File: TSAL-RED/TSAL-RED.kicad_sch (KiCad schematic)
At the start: 41 parts, among them J1 Conn_01x02, J2 Conn_01x02, J5 Conn_02x01, J6 Conn_02x03_Counter_Clockwise, K1 G5V-2, Q1 2N7002, Q2 AO3401A, U1 LM358, U2 4N35, U3 NE555D

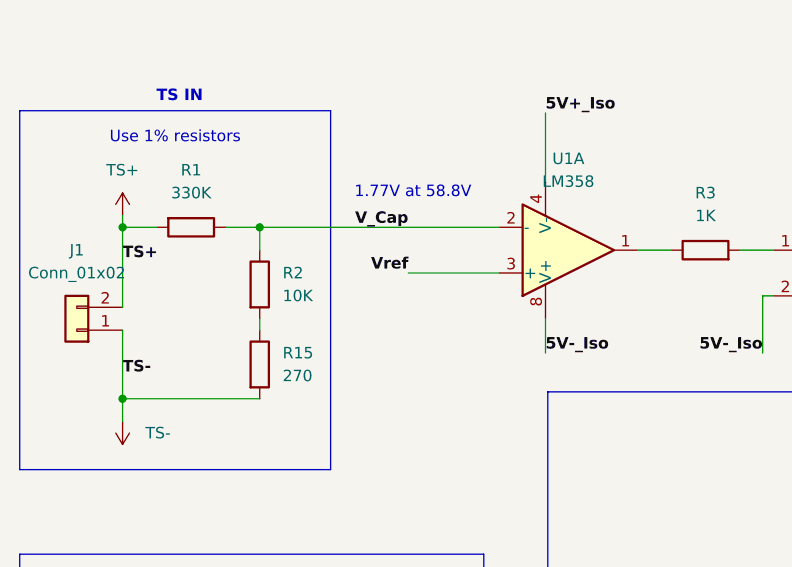
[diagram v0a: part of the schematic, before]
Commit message: Corrected voltage threshold to 50.4V
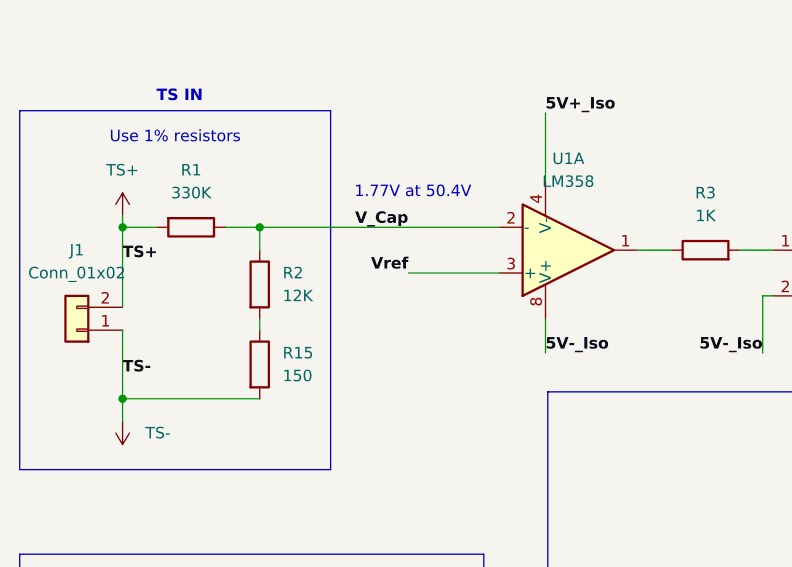
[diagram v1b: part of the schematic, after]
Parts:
- R15: value 270 -> 150
- R2: value 10K -> 12K
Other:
- note added: "1.77V at 50.4V"
- note removed: "1.77V at 58.8V"
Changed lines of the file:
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@@
 		)
 	)
-	(text "1.77V at 58.8V\n"
+	(text "1.77V at 50.4V\n"
 		(exclude_from_sim no)
 		(at 140.208 78.74 0)
@@
 			)
 		)
-		(property "Value" "10K"
+		(property "Value" "12K"
 			(at 125.73 90.1699 0)
 			(effects
@@
 			)
 		)
-		(property "Value" "270"
+		(property "Value" "150"
 			(at 125.73 99.0599 0)
 			(effects

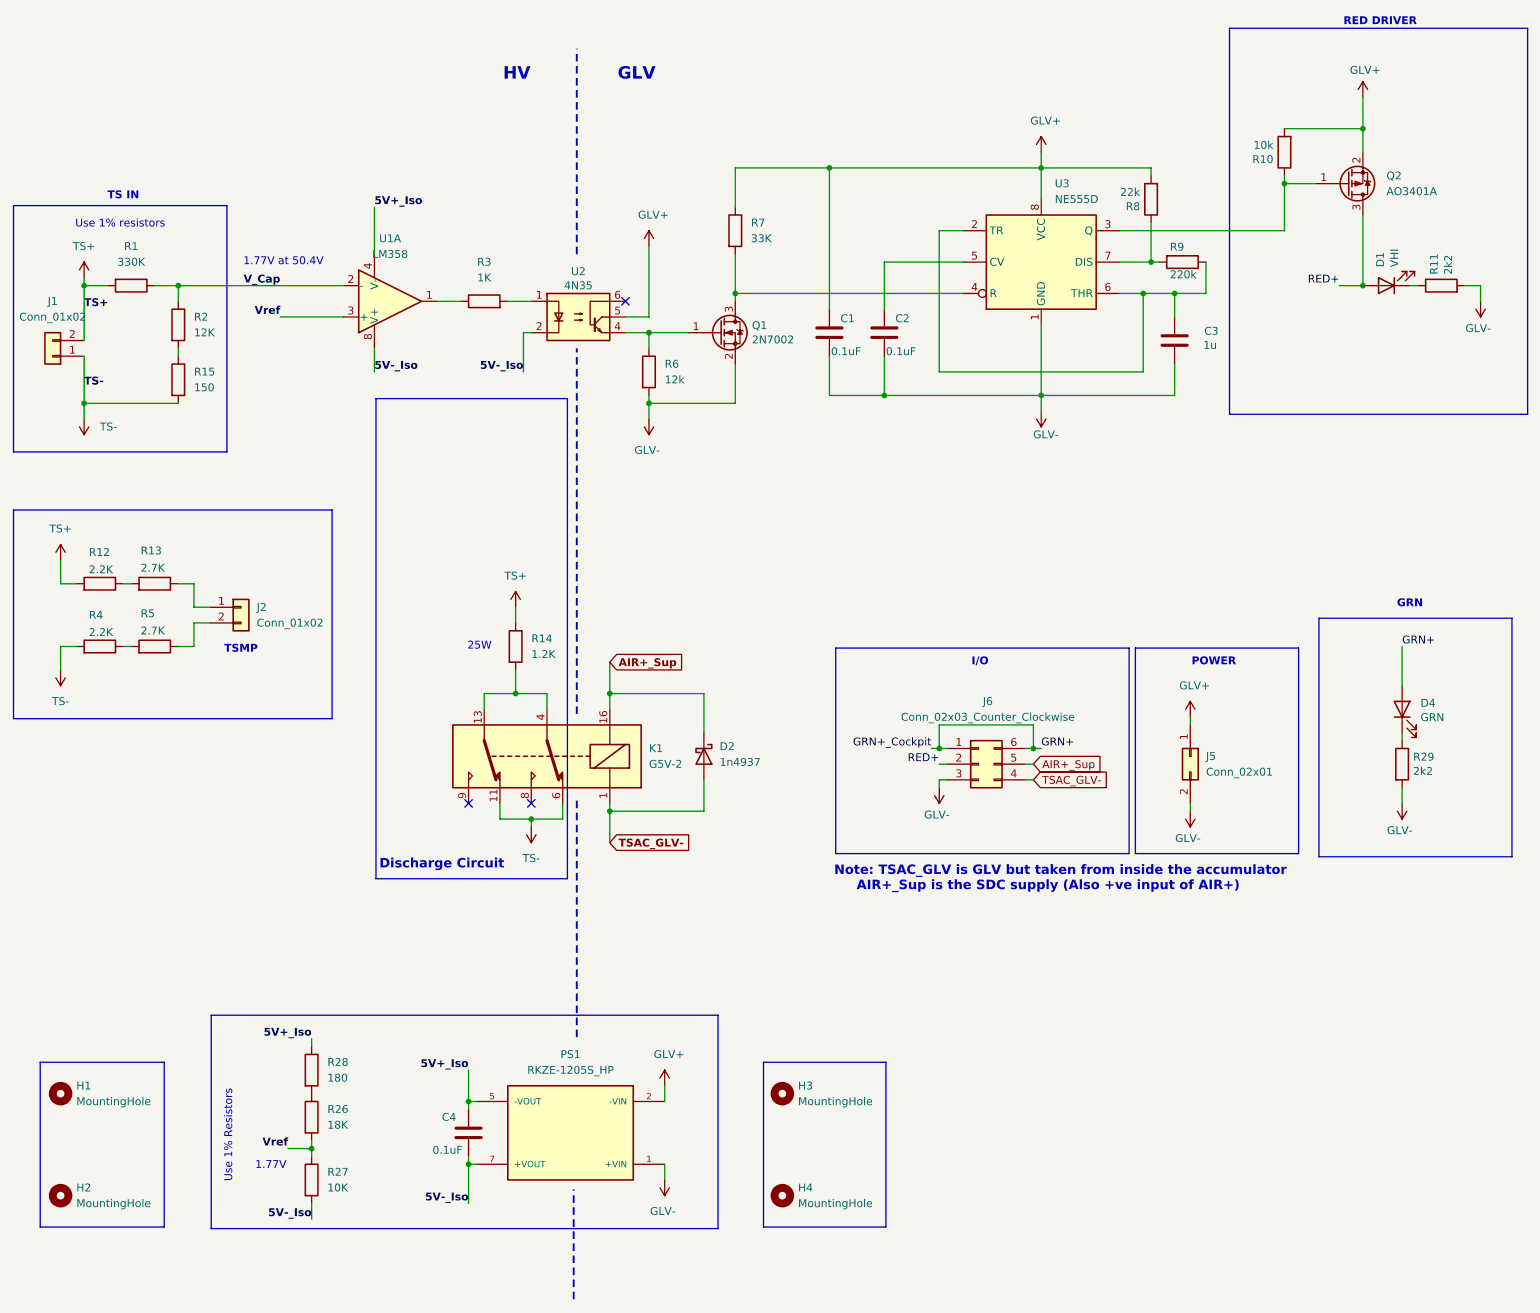
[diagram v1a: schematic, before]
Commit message: added hierarchichal labels for hierarchical sheet compatibility
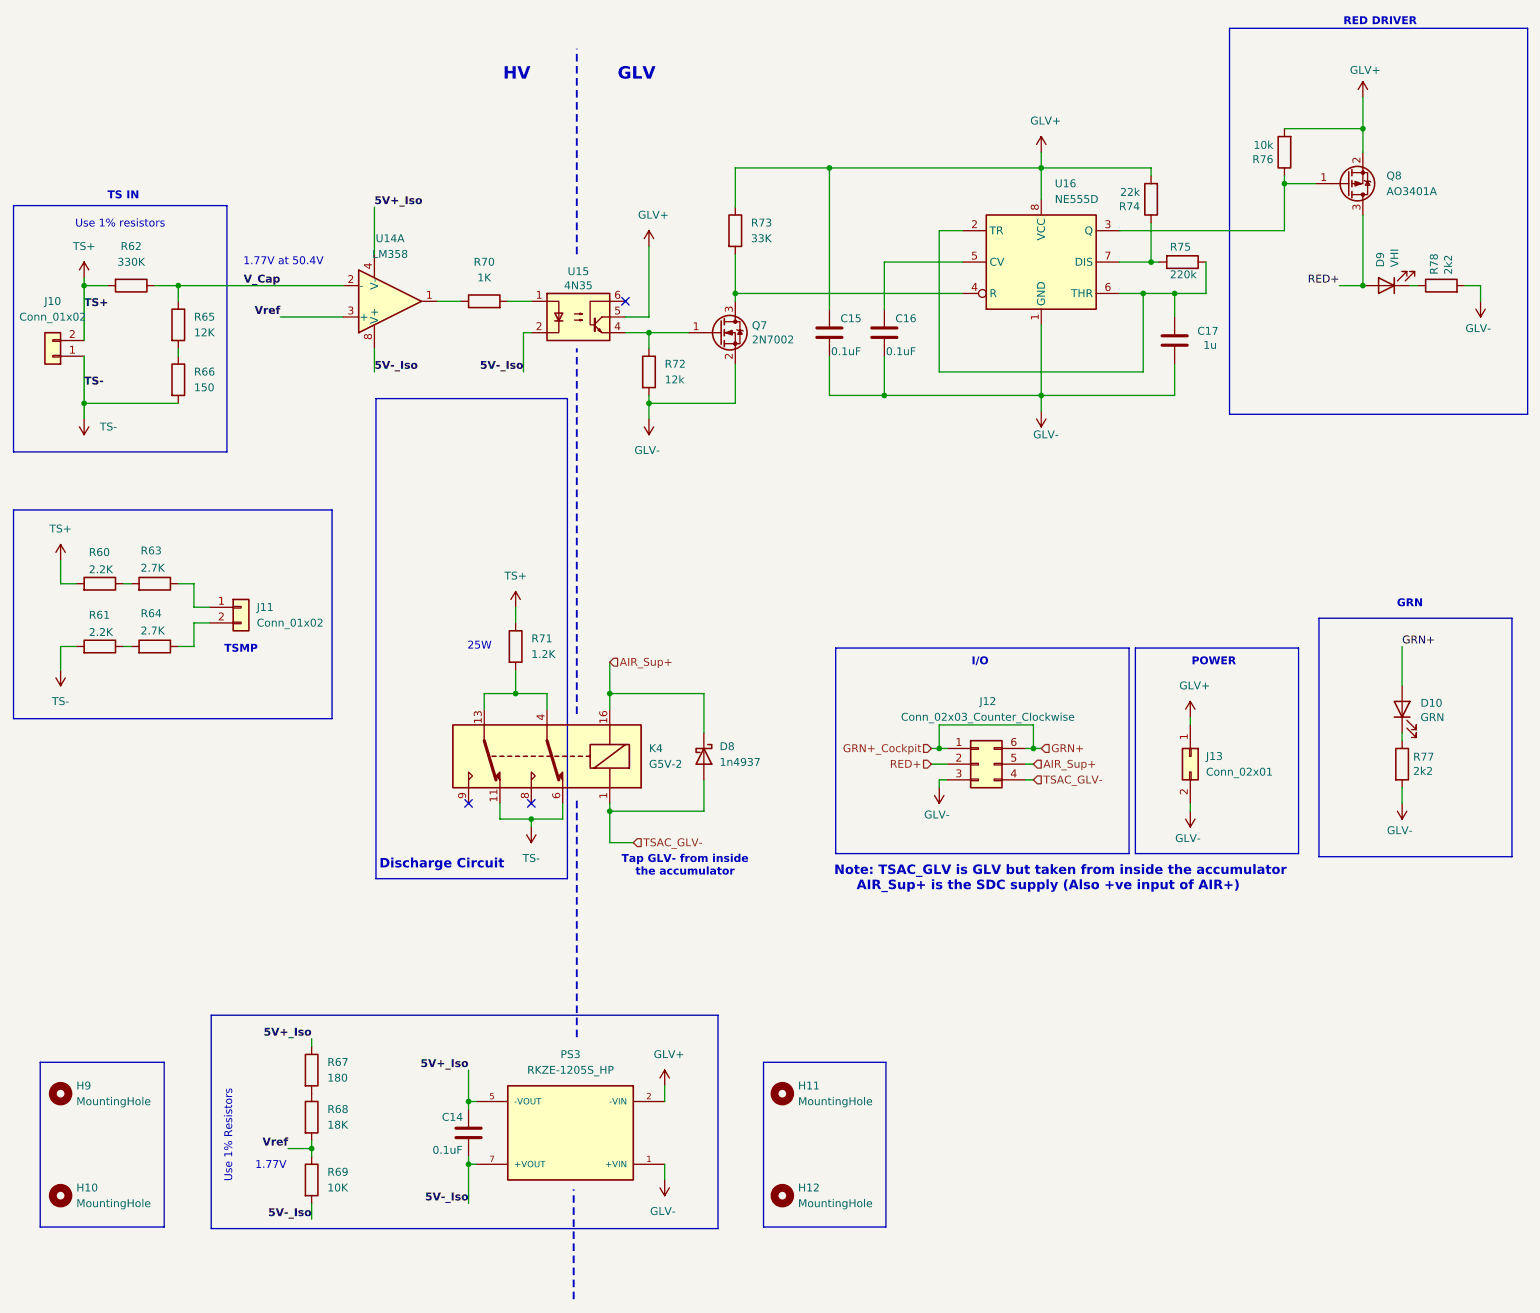
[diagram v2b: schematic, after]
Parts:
- renumbered C4 to C14, C1 to C15, C2 to C16, C3 to C17, D4 to D10, D2 to D8, D1 to D9, H2 to H10, H3 to H11, H4 to H12, H1 to H9, J1 to J10, J2 to J11, J6 to J12, J5 to J13, K1 to K4, PS1 to PS3, Q1 to Q7, Q2 to Q8, R12 to R60, R4 to R61, R1 to R62, R13 to R63, R5 to R64, R2 to R65, R15 to R66, R28 to R67, R26 to R68, R27 to R69, R3 to R70, R14 to R71, R6 to R72, R7 to R73, R8 to R74, R9 to R75, R10 to R76, R29 to R77, R11 to R78, U1 to U14, U2 to U15, U3 to U16
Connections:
- net AIR+_Sup renamed AIR_Sup+
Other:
- note added: "Note: TSAC_GLV is GLV but taken from inside the accumulator AIR_Sup+ is the SDC supply (Also +ve input of AIR+)"
- note added: "Tap GLV- from inside the accumulator"
- note removed: "Note: TSAC_GLV is GLV but taken from inside the accumulator AIR+_Sup is the SDC supply (Also +ve input of AIR+)"

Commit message: Save corrupted files and new modifications
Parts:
- removed D8: 1n4937, Diode_THT:D_DO-41_SOD81_P7.62mm_Horizontal, symbol Diode:1N5819
- removed K4: G5V-2, Relay_THT:Relay_DPDT_Omron_G5V-2, symbol Relay:G5V-2
- added D2: 1N4148, Diode_THT:D_DO-35_SOD27_P7.62mm_Horizontal, symbol Diode:1N4148
- added K2: G2RL-1-E, Relay_THT:Relay_DPDT_Omron_G2RL-2, symbol Relay:G2RL-2
- renumbered C15 to C1, C16 to C2, C17 to C3, C14 to C4, D9 to D1, D10 to D4, H9 to H1, H10 to H2, H11 to H3, H12 to H4, J10 to J1, J11 to J2, J13 to J5, J12 to J6, PS3 to PS1, Q7 to Q1, Q8 to Q2, R62 to R1, R76 to R10, R78 to R11, R60 to R12, R63 to R13, R71 to R14, R66 to R15, R65 to R2, R68 to R26, R69 to R27, R67 to R28, R77 to R29, R70 to R3, R61 to R4, R64 to R5, R72 to R6, R73 to R7, R74 to R8, R75 to R9, U14 to U1, U15 to U2, U16 to U3
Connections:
- net AIR_Sup+: now also D2.1 (K), K2.A2
- net TS-: now also K2.12, K2.22
- net TSAC_GLV-: now also D2.2 (A), K2.A1
- net at R14.2: now also K2.11, K2.21
